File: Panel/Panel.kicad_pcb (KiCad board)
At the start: 2 copper layers, 40 x 128.5 mm, 4 parts

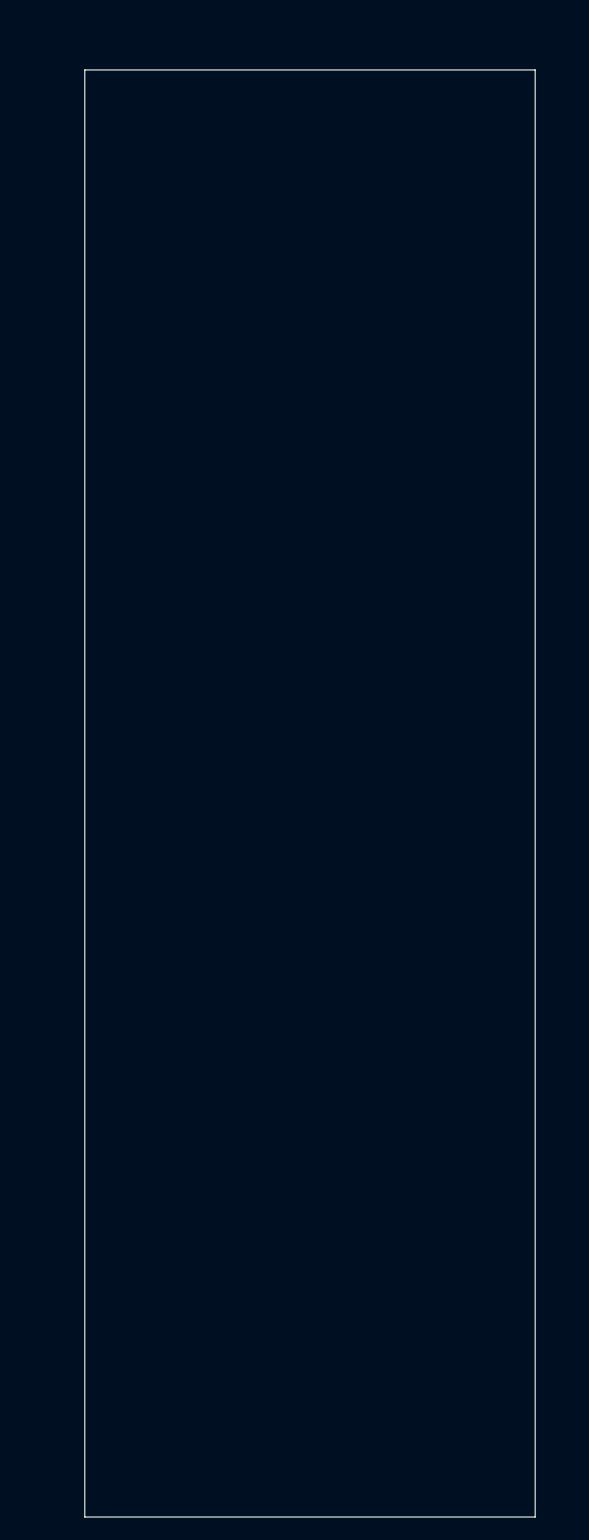
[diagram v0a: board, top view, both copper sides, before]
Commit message: Panel with artwork, holes, cutouts.
Panel size was 8HP shrunk to 6HP.
Logo is too big.
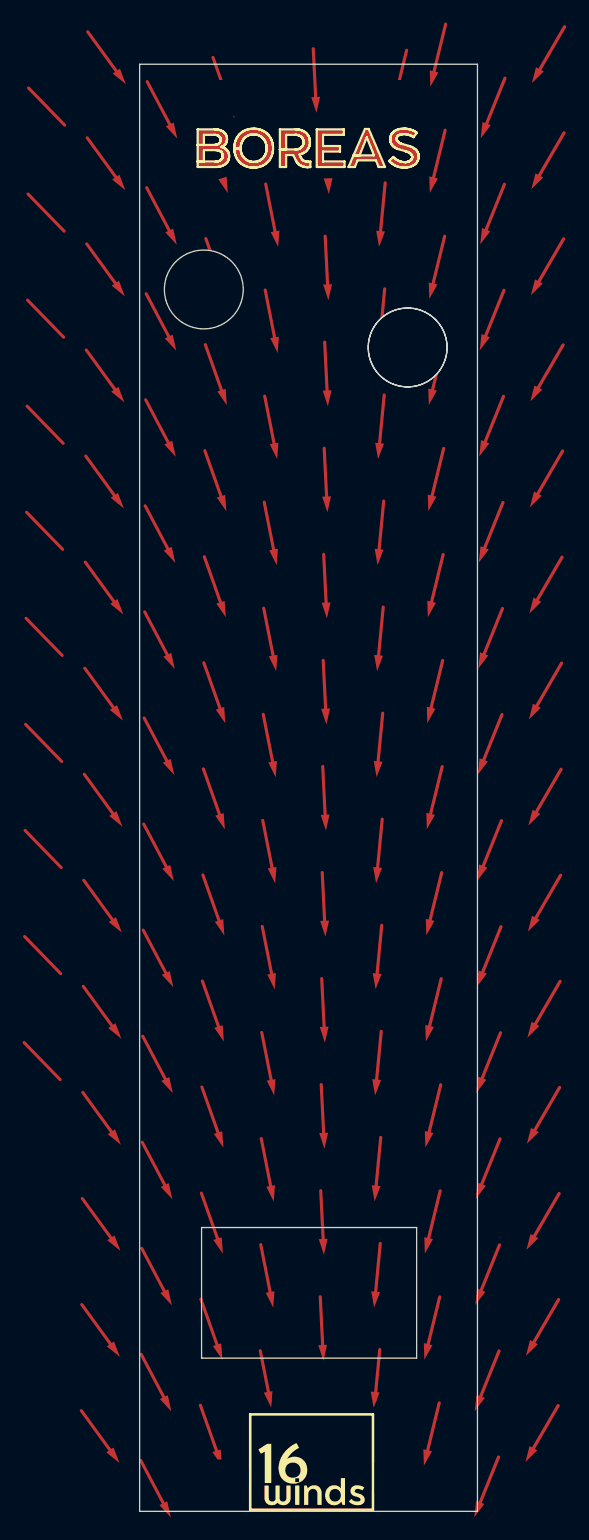
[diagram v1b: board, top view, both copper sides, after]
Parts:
- added ?: , , F.Cu at (68.7, 59.6)
- added REF**: MountingHole, MountingHole:MountingHole_3.2mm_M3, F.Cu at (68.7, 59.6)
- added REF**: MountingHole, MountingHole:MountingHole_3.2mm_M3, F.Cu at (50.6, 54.5)
- moved ? 5.40 mm to (52.4, 160.0)
- moved ? 5.15 mm to (67.4, 37.5)
- moved REF** 4.90 mm to (52.4, 37.5)
- moved ? 4.66 mm to (67.4, 160.0)
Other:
- board size 40 x 128.5 mm -> 30 x 128.5 mm
